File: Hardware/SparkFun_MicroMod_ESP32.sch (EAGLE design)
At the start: 49 parts, among them J1 MICROMOD-2222, Q2 MBT3904DW1T1, U1 W25QXX128MBIT-6X5, U2 ESP32, U4 CP2102N, Y1 40MHz, Y2 32.768kHz

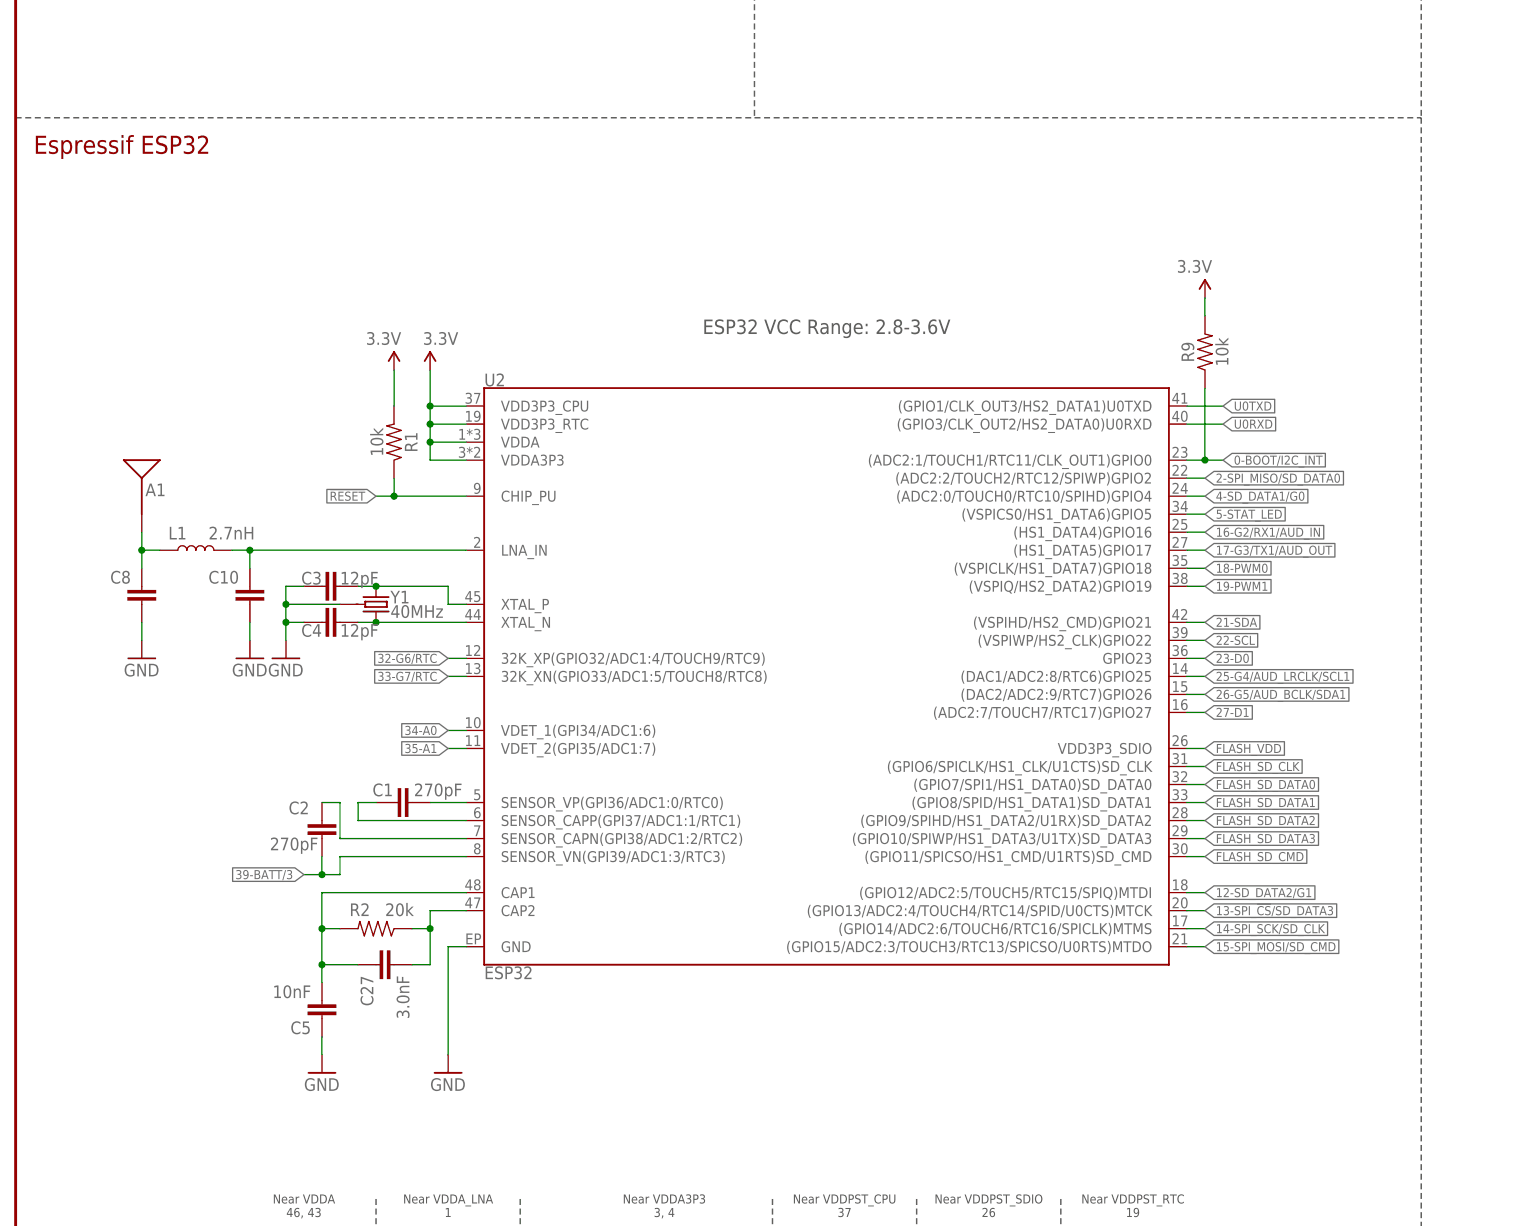
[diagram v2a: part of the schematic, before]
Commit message: Fixed RF trace Width
- Updated RF trace width to 13mil, added calculation to schematic
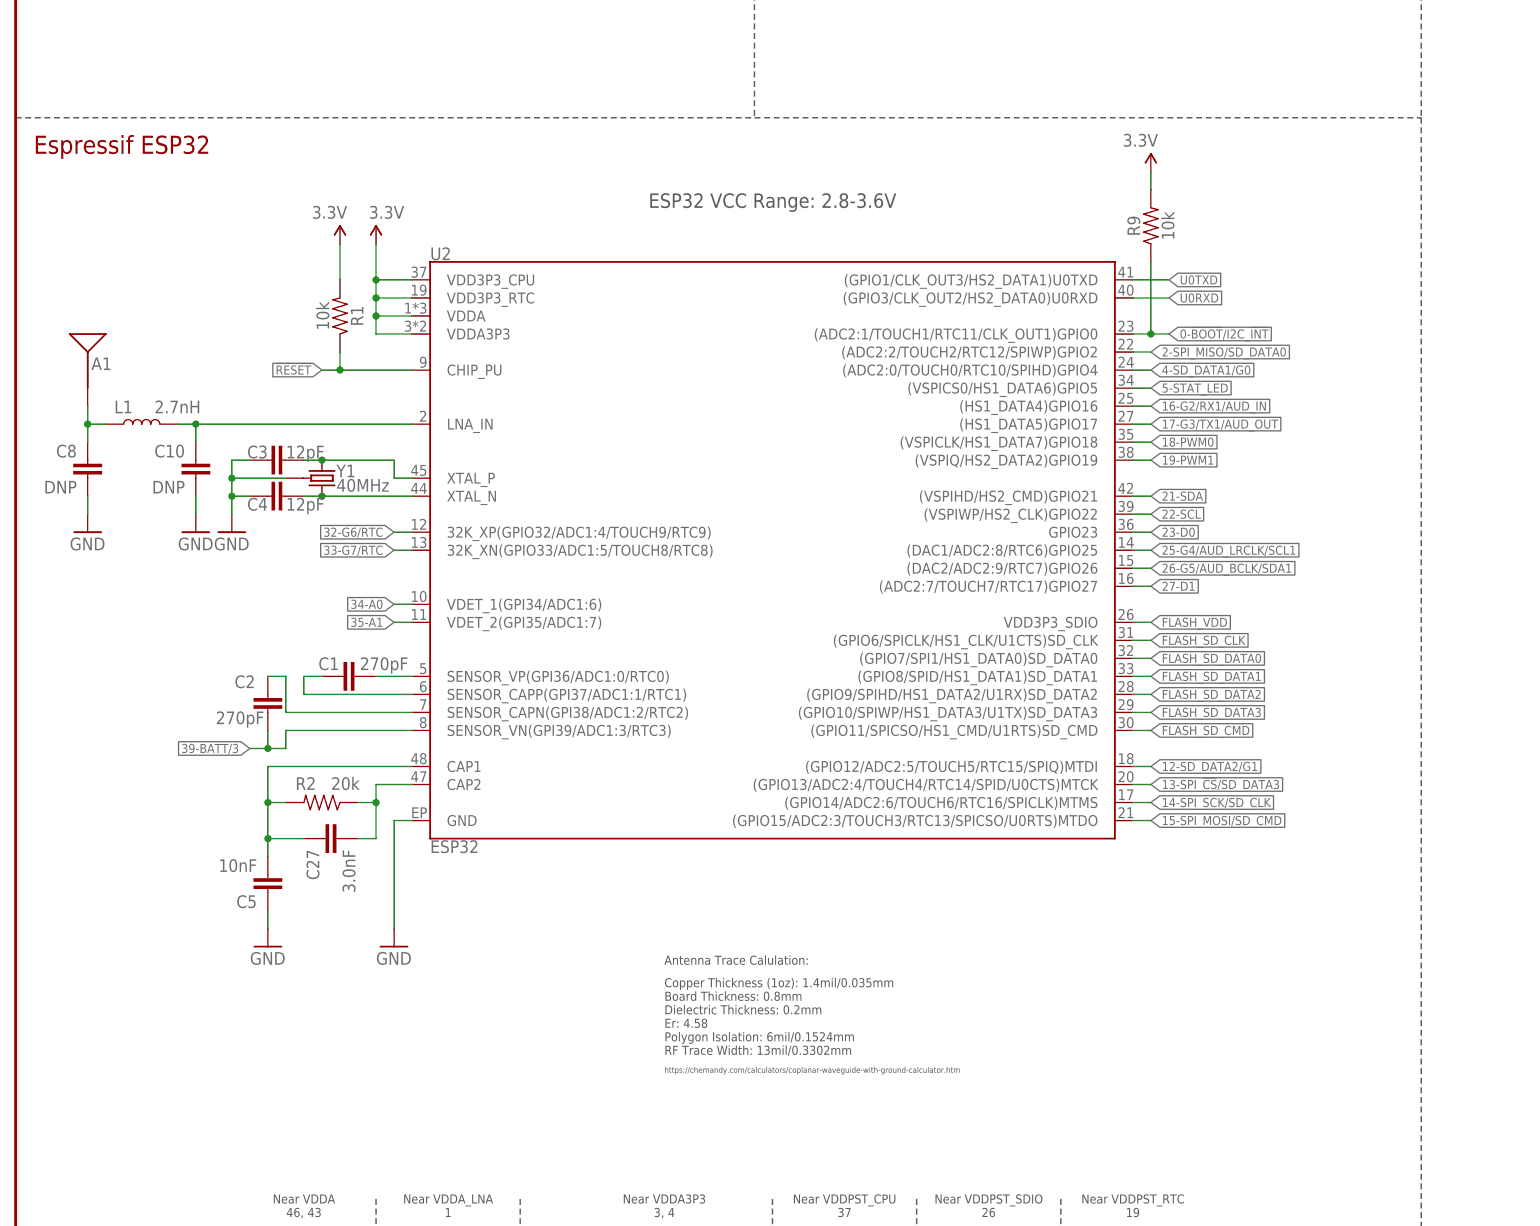
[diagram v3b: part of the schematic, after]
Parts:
- C10, C8: value (none) -> DNP
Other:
- note added: "Antenna Trace Calulation:"
- note added: "Copper Thickness (1oz): 1.4mil/0.035mm Board Thickness: 0.8mm Dielectric Thickness: 0.2mm Er: 4.58 Polygon Isolation: 6mil/0.1524mm RF Trace Width: 13mil/0.3302mm"
- note added: "https://chemandy.com/calculators/coplanar-waveguide-with-ground-calculator.htm"
- moved on the sheet: A1, C1, C10, C2, C27, C3, C4, C5, C8, L1, R1, R2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

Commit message: v02
- Replaced antenna inductor with 0 ohm resistor
- Replaced Flash IC VDD supply from 3.3V power rail to ESP32's FLASH_VDD pin.
- Replaced edge connector to updated pinout
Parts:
- L1: value 2.7nH -> 0; device SparkFun-Coils:INDUCTOR-0402_TIGHT-2.7NH -> SparkFun-Resistors:0OHM-0402T-1/10W
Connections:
- net 3.3V: no longer C17.1, U1.VDD
- net FLASH_VDD: now also C17.1, U1.VDD
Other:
- note added: "v02"
- note removed: "v01"
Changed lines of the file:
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@@
 <?xml version="1.0" encoding="utf-8"?>
 <!DOCTYPE eagle SYSTEM "eagle.dtd">
-<eagle version="9.5.2">
+<eagle version="9.6.0">
 <drawing>
 <settings>
@@
 <layer number="255" name="routoute" color="7" fill="1" visible="yes" active="yes"/>
 </layers>
-<schematic xreflabel="%F%N/%S" xrefpart="/%S.%C%R">
+<schematic xreflabel="%F%N/%S" xrefpart="1_/%S.%C%R">
 <attributes>
 </attributes>
@@
 <part name="GND36" library="SparkFun-PowerSymbols" deviceset="GND" device=""/>
 <part name="C17" library="SparkFun-Capacitors" deviceset="0.1UF" device="-0402T-16V-10%" value="0.1uF"/>
-<part name="SUPPLY3" library="SparkFun-PowerSymbols" deviceset="3.3V" device=""/>
 <part name="FRAME1" library="SparkFun-Aesthetics" deviceset="FRAME-LEDGER" device=""/>
 <part name="R17" library="SparkFun-Resistors" deviceset="10KOHM" device="-0402T-1/16W-1%" value="10k"/>
@@
 <part name="R5" library="SparkFun-Resistors" deviceset="2.2KOHM" device="-0402T-1/16W-1%" value="2.2k"/>
 <part name="U1" library="SparkFun-MicroMod" deviceset="W25QXX" device="128MBIT-6X5"/>
-<part name="L1" library="SparkFun-Coils" deviceset="INDUCTOR" device="-0402_TIGHT-2.7NH" value="2.7nH"/>
+<part name="L1" library="SparkFun-Resistors" deviceset="0OHM" device="-0402T-1/10W" value="0"/>
 <part name="GND12" library="SparkFun-PowerSymbols" deviceset="GND" device=""/>
 <part name="FD1" library="SparkFun-Aesthetics" deviceset="FIDUCIAL" device="UFIDUCIAL" value="FIDUCIALUFIDUCIAL"/>
@@
 <text x="109.22" y="274.32" size="2.54" layer="94" font="vector" rot="MR180" align="top-left">32.768kHz RTC Crystal</text>
 <text x="332.74" y="104.14" size="2.54" layer="94" font="vector" align="top-left">Status LED</text>
-<text x="421.64" y="10.16" size="2.54" layer="94" font="vector" align="top-left">v01</text>
+<text x="421.64" y="10.16" size="2.54" layer="94" font="vector" align="top-left">v02</text>
 <text x="354.838" y="11.43" size="2.54" layer="94" font="vector" rot="MR180" align="top-left">Alex Wende</text>
 <text x="106.68" y="180.34" size="2.032" layer="97" font="vector" align="bottom-center">ESP32 VCC Range: 2.8-3.6V</text>
@@
 <attribute name="VALUE" x="31.496" y="231.521" size="1.778" layer="96" font="vector" rot="MR0"/>
 </instance>
-<instance part="SUPPLY3" gate="G$1" x="33.02" y="243.84" smashed="yes">
-<attribute name="VALUE" x="32.004" y="247.396" size="1.778" layer="96" font="vector"/>
-</instance>
 <instance part="FRAME1" gate="G$1" x="0" y="0" smashed="yes"/>
 <instance part="FRAME1" gate="G$2" x="330.2" y="0" smashed="yes">
@@
 <attribute name="VALUE" x="38.1" y="223.52" size="1.778" layer="96" font="vector"/>
 </instance>
-<instance part="L1" gate="G$1" x="17.78" y="149.86" smashed="yes" rot="R90">
-<attribute name="NAME" x="16.51" y="153.162" size="1.778" layer="95" font="vector" rot="R180"/>
-<attribute name="VALUE" x="19.558" y="153.162" size="1.778" layer="96" font="vector" align="top-left"/>
+<instance part="L1" gate="G$1" x="17.78" y="149.86" smashed="yes">
+<attribute name="NAME" x="19.558" y="152.4" size="1.778" layer="95" font="vector"/>
+<attribute name="VALUE" x="16.256" y="152.4" size="1.778" layer="96" font="vector" rot="R180" align="top-left"/>
 </instance>
 <instance part="GND12" gate="1" x="25.4" y="134.62" smashed="yes">
@@
 <pinref part="SUPPLY2" gate="G$1" pin="3.3V"/>
 <wire x1="45.72" y1="175.26" x2="45.72" y2="170.18" width="0.1524" layer="91"/>
-</segment>
-<segment>
-<pinref part="SUPPLY3" gate="G$1" pin="3.3V"/>
-<pinref part="C17" gate="G$1" pin="1"/>
-<wire x1="33.02" y1="241.3" x2="33.02" y2="243.84" width="0.1524" layer="91"/>
-<wire x1="33.02" y1="238.76" x2="33.02" y2="241.3" width="0.1524" layer="91"/>
-<wire x1="35.56" y1="241.3" x2="33.02" y2="241.3" width="0.1524" layer="91"/>
-<junction x="33.02" y="241.3"/>
-<pinref part="U1" gate="U1" pin="VDD"/>
 </segment>
 <segment>
@@
 <label x="142.24" y="33.02" size="1.27" layer="95" font="vector" rot="R180" xref="yes"/>
 </segment>
-</net>
+<segment>
+<pinref part="C17" gate="G$1" pin="1"/>
+<wire x1="33.02" y1="241.3" x2="33.02" y2="243.84" width="0.1524" layer="91"/>
+<wire x1="33.02" y1="238.76" x2="33.02" y2="241.3" width="0.1524" layer="91"/>
+<wire x1="35.56" y1="241.3" x2="33.02" y2="241.3" width="0.1524" layer="91"/>
+<junction x="33.02" y="241.3"/>
+<pinref part="U1" gate="U1" pin="VDD"/>
+<label x="33.02" y="243.84" size="1.27" layer="95" rot="R90" xref="yes"/>
+</segment>
+</net>

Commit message: v10
- Updated board to v10
- Removed RX and TX test points
- Changed Flash_VDD label to VDD power symbol
- Changed SPI labels to COPI CIPO
- Added vias below antenna
- Moved OSHW logo
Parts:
- removed TP1, TP2: TEST-POINT3, SparkFun-Connectors:TEST-POINT3
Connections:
- net 15-SPI_MOSI/SD_CMD renamed 15-SPI_COPI/SD_CMD
- net 2-SPI_MISO/SD_DATA0 renamed 2-SPI_CIPO/SD_DATA0
- net FLASH_VDD renamed VDD
- net U0RXD: no longer TP1.1
- net U0TXD: no longer TP2.1
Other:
- note added: "v10"
- note removed: "JTAG: - GPIO14 -> TMS - GPIO12 -> TDI - GPIO13 -> TCK - GPIO15 -> TDO"
- note removed: "v02"
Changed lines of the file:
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@@
 <part name="C10" library="SparkFun-Capacitors" deviceset="CAP" device="-0402-TIGHT" value="DNP"/>
 <part name="GND13" library="SparkFun-PowerSymbols" deviceset="GND" device=""/>
-<part name="TP1" library="SparkFun-Connectors" deviceset="TEST-POINT" device="3" value=""/>
-<part name="TP2" library="SparkFun-Connectors" deviceset="TEST-POINT" device="3" value=""/>
+<part name="SUPPLY3" library="SparkFun-PowerSymbols" deviceset="VDD" device=""/>
+<part name="SUPPLY15" library="SparkFun-PowerSymbols" deviceset="VDD" device=""/>
+<part name="SUPPLY18" library="SparkFun-PowerSymbols" deviceset="VDD" device=""/>
 </parts>
 <sheets>
@@
 If U0TXD, GPIO2, GPIO5 are floating,
 GPIO0 determines boot mode</text>
-<text x="332.74" y="190.5" size="2.54" layer="94" font="vector" align="top-left">Auto-Reset</text>
+<text x="332.74" y="187.96" size="2.54" layer="94" font="vector">Auto-Reset</text>
 <text x="40.64" y="38.1" size="1.27" layer="97" font="vector" align="bottom-center">Near VDDA
 46, 43</text>
@@
 <wire x1="330.2" y1="106.68" x2="330.2" y2="193.04" width="0.2032" layer="97" style="longdash"/>
 <wire x1="330.2" y1="106.68" x2="431.8" y2="106.68" width="0.2032" layer="97" style="longdash"/>
-<text x="2.54" y="190.5" size="2.54" layer="94" font="vector" align="top-left">Espressif ESP32</text>
-<text x="2.54" y="276.86" size="2.54" layer="94" font="vector" align="top-left">128Mb Flash</text>
+<text x="2.54" y="187.96" size="2.54" layer="94" font="vector">Espressif ESP32</text>
+<text x="2.54" y="274.32" size="2.54" layer="94" font="vector">128Mb Flash</text>
 <text x="109.22" y="274.32" size="2.54" layer="94" font="vector" rot="MR180" align="top-left">32.768kHz RTC Crystal</text>
 <text x="332.74" y="104.14" size="2.54" layer="94" font="vector" align="top-left">Status LED</text>
-<text x="421.64" y="10.16" size="2.54" layer="94" font="vector" align="top-left">v02</text>
+<text x="421.64" y="7.62" size="2.54" layer="94" font="vector">v10</text>
 <text x="354.838" y="11.43" size="2.54" layer="94" font="vector" rot="MR180" align="top-left">Alex Wende</text>
 <text x="106.68" y="180.34" size="2.032" layer="97" font="vector" align="bottom-center">ESP32 VCC Range: 2.8-3.6V</text>
@@
 <text x="200.66" y="274.32" size="2.54" layer="94" font="vector">MicroMod Connector</text>
 <wire x1="198.12" y1="279.4" x2="198.12" y2="193.04" width="0.2032" layer="97" style="longdash"/>
-<text x="218.44" y="203.2" size="1.27" layer="91" font="vector">JTAG:
-- GPIO14 -&gt; TMS
-- GPIO12 -&gt; TDI
-- GPIO13 -&gt; TCK
-- GPIO15 -&gt; TDO
-</text>
 <text x="91.44" y="73.66" size="1.27" layer="97" font="vector" ratio="16">Antenna Trace Calulation:</text>
 <text x="91.44" y="60.96" size="1.27" layer="97" font="vector">Copper Thickness (1oz): 1.4mil/0.035mm
@@
 <attribute name="VALUE" x="7.62" y="132.08" size="1.778" layer="96" font="vector"/>
 </instance>
-<instance part="TP1" gate="G$1" x="355.6" y="200.66" smashed="yes">
-<attribute name="NAME" x="359.918" y="200.152" size="1.778" layer="95" font="vector"/>
-<attribute name="VALUE" x="353.06" y="198.12" size="1.778" layer="96" font="vector"/>
-</instance>
-<instance part="TP2" gate="G$1" x="355.6" y="198.12" smashed="yes">
-<attribute name="NAME" x="360.172" y="197.104" size="1.778" layer="95" font="vector"/>
-<attribute name="VALUE" x="353.06" y="195.58" size="1.778" layer="96" font="vector"/>
+<instance part="SUPPLY3" gate="VDD" x="33.02" y="243.84" smashed="yes">
+<attribute name="VALUE" x="33.02" y="246.634" size="1.778" layer="96" align="bottom-center"/>
+</instance>
+<instance part="SUPPLY15" gate="VDD" x="187.96" y="124.46" smashed="yes">
+<attribute name="VALUE" x="187.96" y="127.254" size="1.778" layer="96" align="bottom-center"/>
+</instance>
+<instance part="SUPPLY18" gate="VDD" x="137.16" y="30.48" smashed="yes">
+<attribute name="VALUE" x="137.16" y="33.274" size="1.778" layer="96" align="bottom-center"/>
 </instance>
 </instances>
@@
 </segment>
 </net>
-<net name="15-SPI_MOSI/SD_CMD" class="0">
+<net name="15-SPI_COPI/SD_CMD" class="0">
 <segment>
 <wire x1="157.48" y1="93.98" x2="160.02" y2="93.98" width="0.1524" layer="91"/>
@@
 </segment>
 </net>
-<net name="FLASH_VDD" class="0">
-<segment>
-<wire x1="157.48" y1="121.92" x2="160.02" y2="121.92" width="0.1524" layer="91"/>
-<label x="160.02" y="121.92" size="1.27" layer="95" font="vector" xref="yes"/>
+<net name="VDD" class="0">
+<segment>
 <pinref part="U2" gate="G$1" pin="VDD3P3_SDIO"/>
+<pinref part="SUPPLY15" gate="VDD" pin="VDD"/>
+<wire x1="187.96" y1="124.46" x2="187.96" y2="121.92" width="0.1524" layer="91"/>
+<wire x1="187.96" y1="121.92" x2="157.48" y2="121.92" width="0.1524" layer="91"/>
 </segment>
 <segment>
 <pinref part="C24" gate="G$1" pin="1"/>
-<wire x1="137.16" y1="27.94" x2="137.16" y2="30.48" width="0.1524" layer="91"/>
-<wire x1="137.16" y1="30.48" x2="144.78" y2="30.48" width="0.1524" layer="91"/>
-<wire x1="144.78" y1="30.48" x2="144.78" y2="33.02" width="0.1524" layer="91"/>
-<wire x1="144.78" y1="33.02" x2="142.24" y2="33.02" width="0.1524" layer="91"/>
-<label x="142.24" y="33.02" size="1.27" layer="95" font="vector" rot="R180" xref="yes"/>
+<pinref part="SUPPLY18" gate="VDD" pin="VDD"/>
+<wire x1="137.16" y1="30.48" x2="137.16" y2="27.94" width="0.1524" layer="91"/>
 </segment>
 <segment>
 <pinref part="C17" gate="G$1" pin="1"/>
-<wire x1="33.02" y1="241.3" x2="33.02" y2="243.84" width="0.1524" layer="91"/>
 <wire x1="33.02" y1="238.76" x2="33.02" y2="241.3" width="0.1524" layer="91"/>
 <wire x1="35.56" y1="241.3" x2="33.02" y2="241.3" width="0.1524" layer="91"/>
 <junction x="33.02" y="241.3"/>
 <pinref part="U1" gate="U1" pin="VDD"/>
-<label x="33.02" y="243.84" size="1.27" layer="95" rot="R90" xref="yes"/>
+<pinref part="SUPPLY3" gate="VDD" pin="VDD"/>
+<wire x1="33.02" y1="243.84" x2="33.02" y2="241.3" width="0.1524" layer="91"/>
 </segment>
 </net>
@@
 </segment>
 </net>
-<net name="2-SPI_MISO/SD_DATA0" class="0">
+<net name="2-SPI_CIPO/SD_DATA0" class="0">
 <segment>
 <wire x1="157.48" y1="160.02" x2="160.02" y2="160.02" width="0.1524" layer="91"/>
@@
 <label x="411.48" y="248.92" size="1.27" layer="95" font="vector" xref="yes"/>
 </segment>
-<segment>
-<pinref part="TP1" gate="G$1" pin="1"/>
-<wire x1="355.6" y1="200.66" x2="353.06" y2="200.66" width="0.1524" layer="91"/>
-<label x="353.06" y="200.66" size="1.27" layer="95" font="vector" rot="R180" xref="yes"/>
-</segment>
 </net>
 <net name="U0TXD" class="0">
@@
 <label x="411.48" y="246.38" size="1.27" layer="95" font="vector" xref="yes"/>
 </segment>
-<segment>
-<pinref part="TP2" gate="G$1" pin="1"/>
-<wire x1="355.6" y1="198.12" x2="353.06" y2="198.12" width="0.1524" layer="91"/>
-<label x="353.06" y="198.12" size="1.27" layer="95" font="vector" rot="R180" xref="yes"/>
-</segment>
-</net>
+</net>
